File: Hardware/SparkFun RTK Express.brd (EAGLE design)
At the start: 68.2 x 110.1 mm, 168 parts, among them J13 Internal, J17 Qwiic Right Angle, J19 MICRO-SD-PUSH-PUSH-EXT-PIN, J3 USB Female Type C Connector, J4 External, J5 USB Female Type C Connector, Q1 SIL2308-TP, Q2 MBT3904DW1T1, U1 74HC4052D, U10 MCP73833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

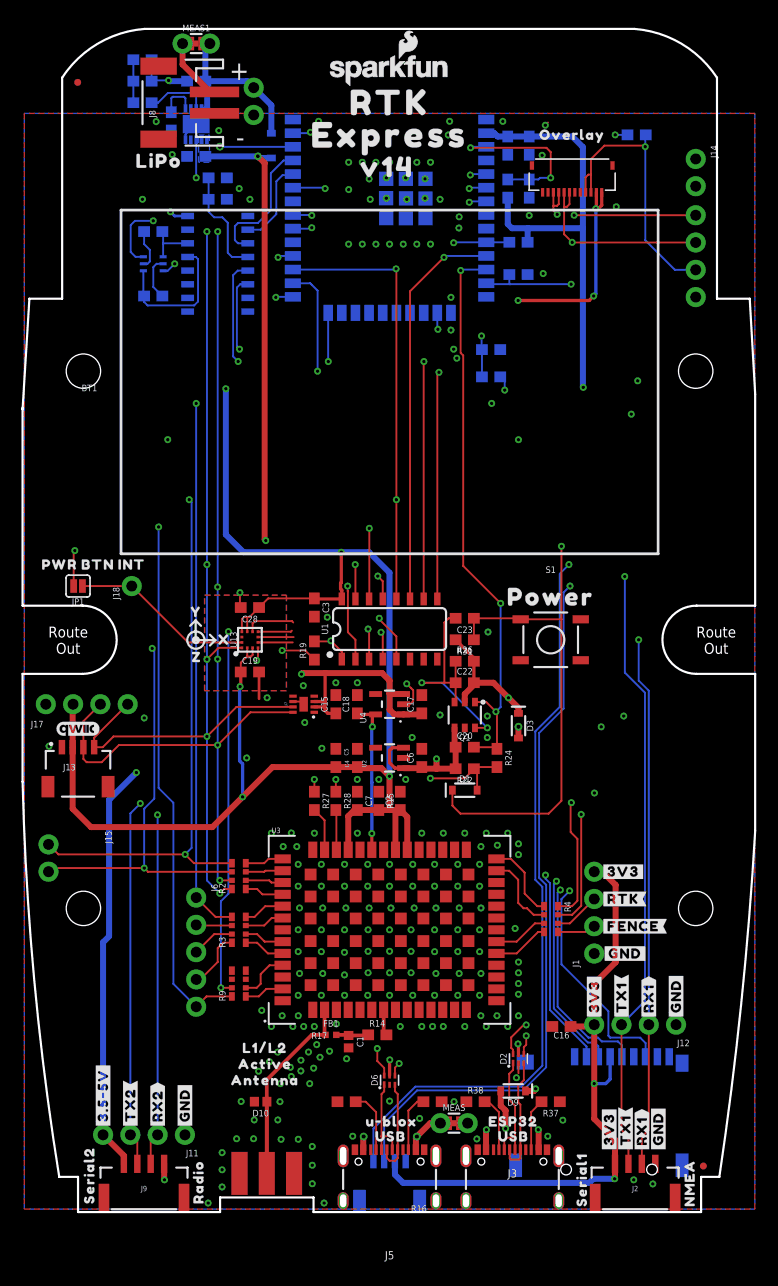
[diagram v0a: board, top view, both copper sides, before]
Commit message: LIF overlay connector, accel plane removal, full ESP32 FP.
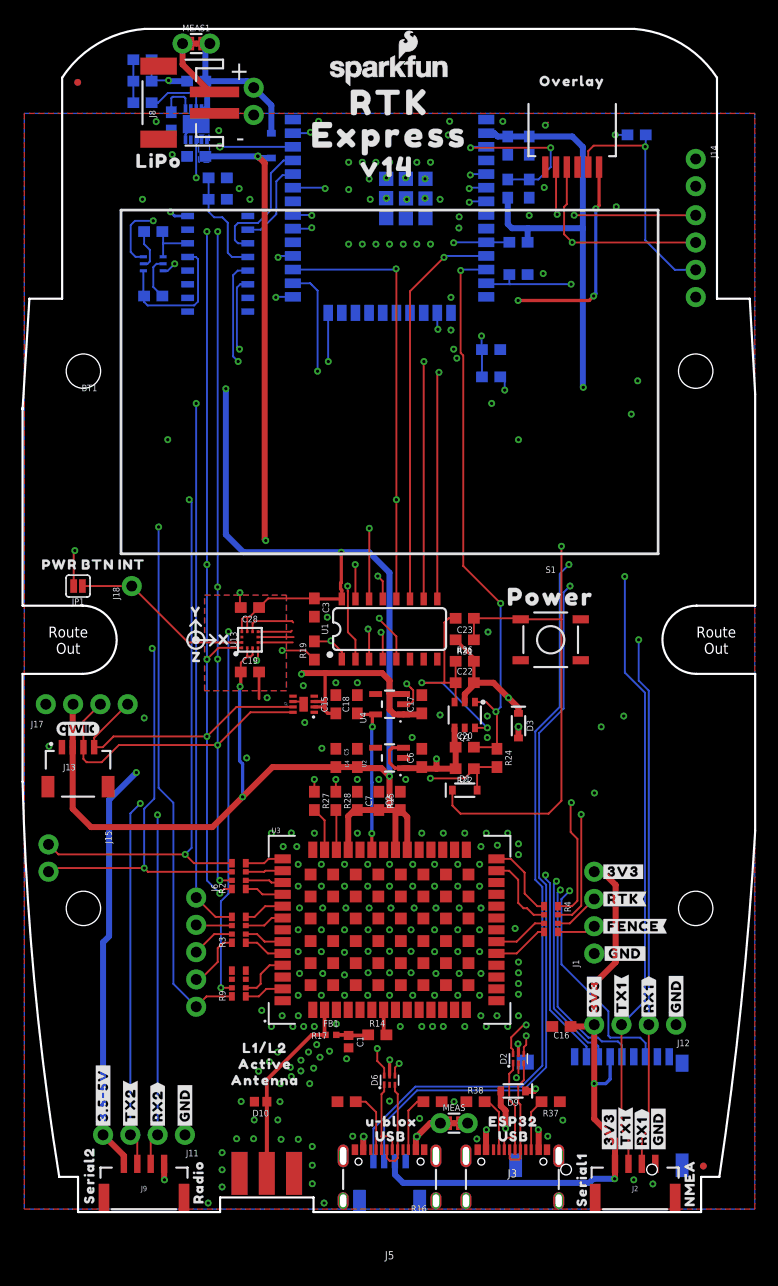
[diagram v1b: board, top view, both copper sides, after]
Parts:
- removed J20: (no value), SparkFun-Connectors:FPC_12_0.5MM
- removed R18: 10k, SparkFun-Resistors:0603@1
- added JP2: CONN_06, 1mm Pitch Connector:FPC_6_1MM-LIF
- added R6: 10k, SparkFun-Resistors:0603
- moved U$8 5.00 mm to (52.0, 105.0)
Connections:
- net CHG_LED_RES: now also JP2.2; no longer J20.3, J20.4
- net CHG_THERM1: now also R6.2; no longer R18.2
- net ESP_14/SETUP_BUTTON: now also JP2.4; no longer J20.7, J20.8
- net GND: now also JP2.6, R6.1; no longer J20.11, J20.12, R18.1
- net POWER_BTN: now also JP2.5; no longer J20.10, J20.9
- net V_USB: now also JP2.1; no longer J20.1, J20.2
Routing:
- net CHG_LED_RES: track 26.4 -> 22.7 mm
- net ESP32_EN: track 76.0 -> 78.2 mm
- net ESP_14/SETUP_BUTTON: track 31.0 -> 31.7 mm
- net POWER_BTN: track 143.0 -> 143.6 mm
- net V_USB: track 189.7 -> 190.2 mm
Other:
- board text added: "ENIG Finish"
- board text removed: "11.9+2.75=14.65mm"
- board text removed: "11.9-3.4=8.5mm actuator length on square button"
- board text removed: "11.9-8=3.9"
- board text removed: "18.5-5-1.6=11.9mm"
- board text removed: "Distance from PCB surface to outer surface of lid:"
- board text removed: "Distance from inner lid to PCB surface:"

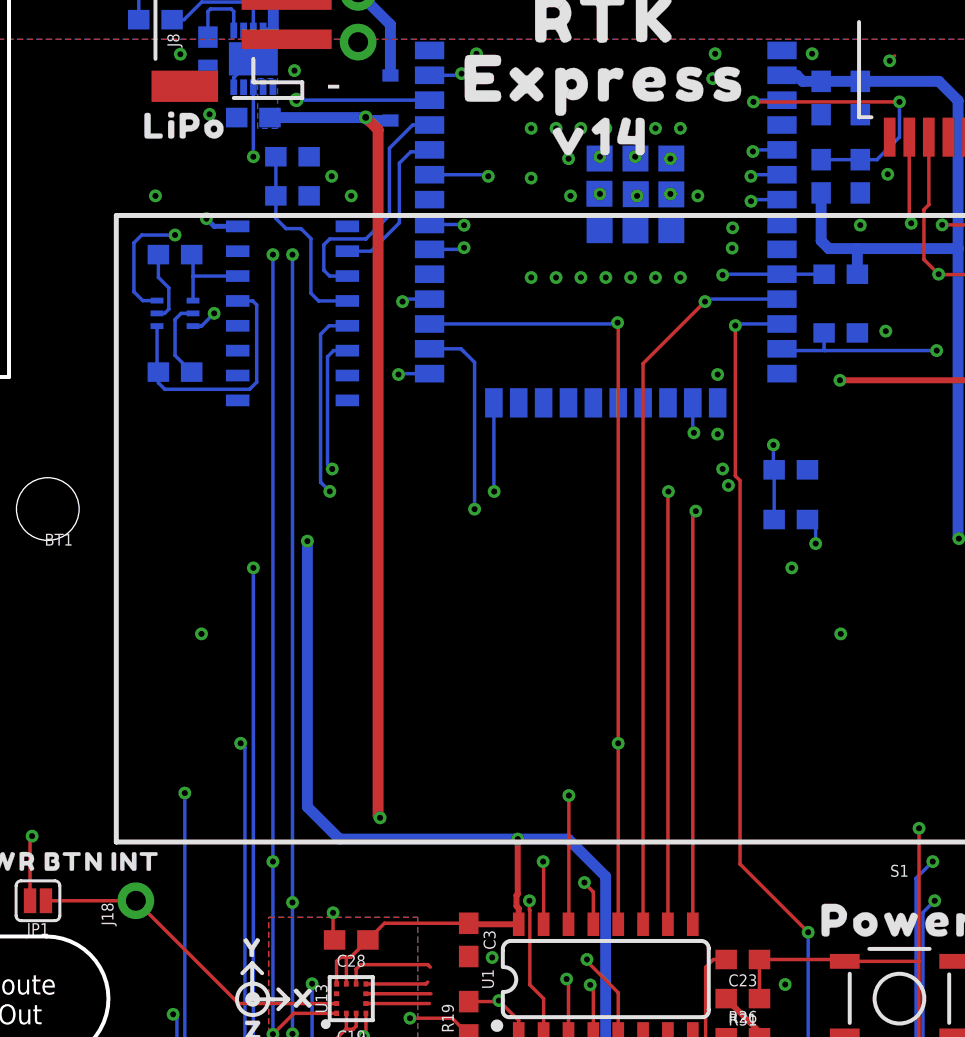
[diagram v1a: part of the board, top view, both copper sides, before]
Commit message: v15. Fix tCream on LIF connector. Correct CH340 3.3V.
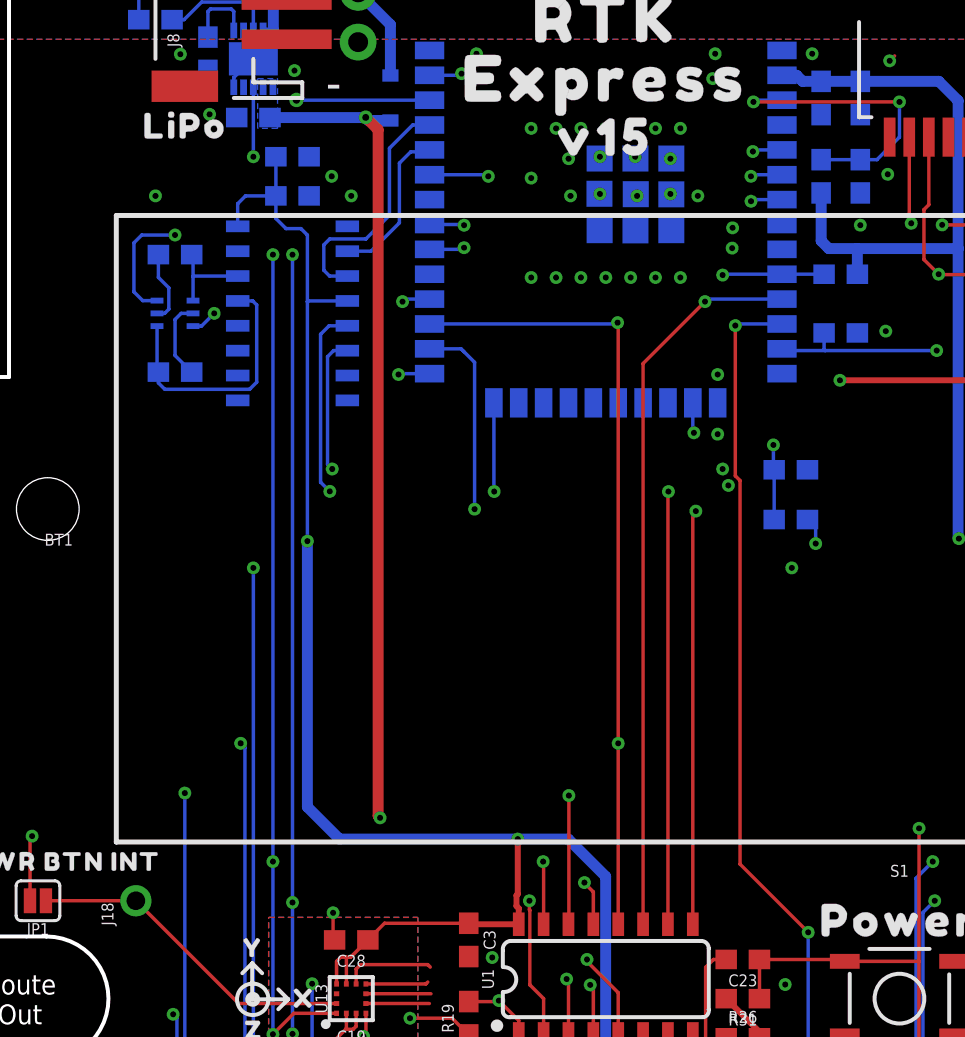
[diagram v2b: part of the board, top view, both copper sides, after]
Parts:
- removed U$12: (no value), output:V140
- added U$18: (no value), output:V150
- J19: value MICRO-SD-PUSH-PUSH-EXT-PIN -> MICROSD
- JP2: value CONN_06 -> (none); device 1mm Pitch Connector:FPC_6_1MM-LIF -> SparkFun-Connectors:FPC_6_1MM-LIF
- MEAS, MEAS1: value JUMPER-COMBO_2_NC_TRACE -> (none)
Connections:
- removed net N$1: C13.1, C14.1, U6.4
- net 3.3V: now also C13.1, C14.1, U6.16, U6.4
- net V_USB: no longer U6.16
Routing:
- net V_USB: track 190.2 -> 134.5 mm, vias 12 -> 9
- net 3.3V: track 308.1 -> 334.2 mm
- net N$1: track 10.2 -> 0.00 mm
- net ESP_I39/ADC39: track 60.8 -> 58.6 mm
- net ESP_I34/ZED_TX_READY: track 103.0 -> 100.7 mm
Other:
- board text added: "N. Seidle"
- board text added: "Red Soldermask"

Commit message: Production files for v15
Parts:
- moved JP2 2.00 mm to (52.0, 98.0)
- moved U$8 2.00 mm to (52.0, 103.0)
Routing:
- net V_USB: track 134.5 -> 132.5 mm
- net POWER_BTN: track 143.6 -> 141.6 mm
- net ESP_14/SETUP_BUTTON: track 31.7 -> 29.7 mm
- net CHG_LED_RES: track 22.7 -> 24.7 mm
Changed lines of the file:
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@@
 <setting verticaltext="up"/>
 </settings>
-<grid distance="0.05" unitdist="inch" unit="inch" style="lines" multiple="1" display="yes" altdistance="0.005" altunitdist="inch" altunit="inch"/>
+<grid distance="1" unitdist="mm" unit="mm" style="lines" multiple="1" display="yes" altdistance="0.1" altunitdist="mm" altunit="mm"/>
 <layers>
 <layer number="1" name="Top/Horz" color="4" fill="1" visible="yes" active="yes"/>
@@
 <layer number="23" name="tOrigins" color="15" fill="1" visible="yes" active="yes"/>
 <layer number="24" name="bOrigins" color="15" fill="1" visible="yes" active="yes"/>
-<layer number="25" name="tNames" color="7" fill="1" visible="yes" active="yes"/>
-<layer number="26" name="bNames" color="7" fill="1" visible="yes" active="yes"/>
-<layer number="27" name="tValues" color="7" fill="1" visible="yes" active="yes"/>
-<layer number="28" name="bValues" color="7" fill="1" visible="yes" active="yes"/>
-<layer number="29" name="tStop" color="7" fill="3" visible="yes" active="yes"/>
-<layer number="30" name="bStop" color="7" fill="6" visible="yes" active="yes"/>
-<layer number="31" name="tCream" color="7" fill="4" visible="yes" active="yes"/>
-<layer number="32" name="bCream" color="7" fill="5" visible="yes" active="yes"/>
-<layer number="33" name="tFinish" color="6" fill="3" visible="yes" active="yes"/>
-<layer number="34" name="bFinish" color="6" fill="6" visible="yes" active="yes"/>
-<layer number="35" name="tGlue" color="7" fill="4" visible="yes" active="yes"/>
-<layer number="36" name="bGlue" color="7" fill="5" visible="yes" active="yes"/>
-<layer number="37" name="tTest" color="7" fill="1" visible="yes" active="yes"/>
-<layer number="38" name="bTest" color="7" fill="1" visible="yes" active="yes"/>
-<layer number="39" name="tKeepout" color="4" fill="11" visible="yes" active="yes"/>
-<layer number="40" name="bKeepout" color="1" fill="11" visible="yes" active="yes"/>
-<layer number="41" name="tRestrict" color="4" fill="10" visible="yes" active="yes"/>
-<layer number="42" name="bRestrict" color="1" fill="10" visible="yes" active="yes"/>
-<layer number="43" name="vRestrict" color="2" fill="10" visible="yes" active="yes"/>
-<layer number="44" name="Drills" color="7" fill="1" visible="yes" active="yes"/>
+<layer number="25" name="tNames" color="7" fill="1" visible="no" active="yes"/>
+<layer number="26" name="bNames" color="7" fill="1" visible="no" active="yes"/>
+<layer number="27" name="tValues" color="7" fill="1" visible="no" active="yes"/>
+<layer number="28" name="bValues" color="7" fill="1" visible="no" active="yes"/>
+<layer number="29" name="tStop" color="7" fill="3" visible="no" active="yes"/>
+<layer number="30" name="bStop" color="7" fill="6" visible="no" active="yes"/>
+<layer number="31" name="tCream" color="7" fill="4" visible="no" active="yes"/>
+<layer number="32" name="bCream" color="7" fill="5" visible="no" active="yes"/>
+<layer number="33" name="tFinish" color="6" fill="3" visible="no" active="yes"/>
+<layer number="34" name="bFinish" color="6" fill="6" visible="no" active="yes"/>
+<layer number="35" name="tGlue" color="7" fill="4" visible="no" active="yes"/>
+<layer number="36" name="bGlue" color="7" fill="5" visible="no" active="yes"/>
+<layer number="37" name="tTest" color="7" fill="1" visible="no" active="yes"/>
+<layer number="38" name="bTest" color="7" fill="1" visible="no" active="yes"/>
+<layer number="39" name="tKeepout" color="4" fill="11" visible="no" active="yes"/>
+<layer number="40" name="bKeepout" color="1" fill="11" visible="no" active="yes"/>
+<layer number="41" name="tRestrict" color="4" fill="10" visible="no" active="yes"/>
+<layer number="42" name="bRestrict" color="1" fill="10" visible="no" active="yes"/>
+<layer number="43" name="vRestrict" color="2" fill="10" visible="no" active="yes"/>
+<layer number="44" name="Drills" color="7" fill="1" visible="no" active="yes"/>
 <layer number="45" name="Holes" color="7" fill="1" visible="yes" active="yes"/>
-<layer number="46" name="Milling" color="3" fill="1" visible="yes" active="yes"/>
-<layer number="47" name="Measures" color="7" fill="1" visible="yes" active="yes"/>
-<layer number="48" name="Document" color="7" fill="1" visible="yes" active="yes"/>
-<layer number="49" name="Reference" color="7" fill="1" visible="yes" active="yes"/>
-<layer number="50" name="dxf" color="7" fill="1" visible="yes" active="yes"/>
+<layer number="46" name="Milling" color="3" fill="1" visible="no" active="yes"/>
+<layer number="47" name="Measures" color="7" fill="1" visible="no" active="yes"/>
+<layer number="48" name="Document" color="7" fill="1" visible="no" active="yes"/>
+<layer number="49" name="Reference" color="7" fill="1" visible="no" active="yes"/>
+<layer number="50" name="dxf" color="7" fill="1" visible="no" active="yes"/>
 <layer number="51" name="tDocu" color="6" fill="1" visible="yes" active="yes"/>
-<layer number="52" name="bDocu" color="7" fill="1" visible="yes" active="yes"/>
+<layer number="52" name="bDocu" color="7" fill="1" visible="no" active="yes"/>
 <layer number="91" name="Nets" color="2" fill="1" visible="no" active="no"/>
 <layer number="92" name="Busses" color="1" fill="1" visible="no" active="no"/>
@@
 <element name="U$4" library="output" package="INT0" value="" x="11" y="60" smashed="yes"/>
 <element name="U$9" library="output" package="PWR_BTN1" value="" x="6" y="60" smashed="yes"/>
-<element name="U$8" library="output" package="OVERLAY0" value="" x="52" y="105" smashed="yes"/>
+<element name="U$8" library="output" package="OVERLAY0" value="" x="52" y="103" smashed="yes"/>
 <element name="D10" library="SparkFun-DiscreteSemi" package="0402" value="PESD0402-0402" x="23" y="10" smashed="yes" rot="R180">
 <attribute name="DIGIKEY_PART" value="PESD0402-140CT-ND" x="23" y="10" size="1.778" layer="27" font="vector" ratio="15" rot="R180" display="off"/>
@@
 <attribute name="VALUE" value="10k" x="44.45" y="78.232" size="0.6096" layer="28" font="vector" ratio="20" rot="MR180" align="top-center"/>
 </element>
-<element name="JP2" library="SparkFun-Connectors" package="FPC_6_1MM-LIF" value="" x="52" y="100" smashed="yes" rot="R180">
-<attribute name="PROD_ID" value="CONN-16692" x="52" y="100" size="1.778" layer="27" rot="R180" display="off"/>
+<element name="JP2" library="SparkFun-Connectors" package="FPC_6_1MM-LIF" value="" x="52" y="98" smashed="yes" rot="R180">
+<attribute name="PROD_ID" value="CONN-16692" x="52" y="98" size="1.778" layer="27" rot="R180" display="off"/>
 </element>
 <element name="R6" library="SparkFun-Resistors" package="0603" value="10k" x="12" y="107" smashed="yes" rot="MR0">
@@
 <contactref element="S1" pad="3"/>
 <via x="57.5" y="74.0031" extent="1-16" drill="0.3048"/>
-<via x="49.4" y="95.1031" extent="1-16" drill="0.3048"/>
+<via x="49.5" y="92.3031" extent="1-16" drill="0.3048"/>
 <via x="32" y="49" extent="1-16" drill="0.3048"/>
 <via x="36.6" y="48.9" extent="1-16" drill="0.3048"/>
@@
 <wire x1="44.09" y1="86.1" x2="44.323" y2="86.1" width="0.3048" layer="16"/>
 <contactref element="JP2" pad="4"/>
-<wire x1="51.5" y1="97" x2="51.5" y2="93.55" width="0.1778" layer="1"/>
+<wire x1="51.5" y1="95" x2="51.5" y2="93.55" width="0.1778" layer="1"/>
 <wire x1="51.5" y1="93.55" x2="51.25" y2="93.3" width="0.1778" layer="1"/>
 </signal>
@@
 <contactref element="JP2" pad="2"/>
 <contactref element="R1" pad="1"/>
-<wire x1="53.5" y1="97" x2="53.5" y2="98.5" width="0.1778" layer="1"/>
+<wire x1="53.5" y1="95" x2="53.5" y2="98.5" width="0.1778" layer="1"/>
 <wire x1="53.5" y1="98.5" x2="54" y2="99" width="0.1778" layer="1"/>
 <wire x1="54" y1="99" x2="58.7" y2="99" width="0.1778" layer="1"/>
@@
 <wire x1="51" y1="61.7" x2="51" y2="92.52" width="0.1778" layer="15"/>
 <contactref element="JP2" pad="5"/>
-<wire x1="50.5" y1="97" x2="50.5" y2="92.7" width="0.1778" layer="1"/>
+<wire x1="50.5" y1="95" x2="50.5" y2="92.7" width="0.1778" layer="1"/>
 <wire x1="50.5" y1="92.7" x2="50.6" y2="92.6" width="0.1778" layer="1"/>
 </signal>
@@
 <wire x1="35" y1="12.43" x2="35" y2="13.874" width="0.3048" layer="1"/>
 <wire x1="35" y1="13.874" x2="35.02" y2="13.894" width="0.3048" layer="1"/>
-<wire x1="47" y1="44.9" x2="47" y2="71.628" width="0.3048" layer="15"/>
-<wire x1="47" y1="71.628" x2="47" y2="84.5424" width="0.3048" layer="15"/>
+<wire x1="47" y1="44.9" x2="47" y2="84.5424" width="0.3048" layer="15"/>
 <wire x1="47" y1="84.5424" x2="46.9604" y2="84.582" width="0.3048" layer="15"/>
 <via x="46.9604" y="84.582" extent="1-16" drill="0.3048"/>
@@
 <wire x1="54.2" y1="85.2" x2="54" y2="85" width="0.3048" layer="16"/>
 <contactref element="JP2" pad="1"/>
-<wire x1="54.5" y1="97" x2="54.5" y2="93.4169" width="0.3048" layer="1"/>
+<wire x1="54.5" y1="95" x2="54.5" y2="93.4169" width="0.3048" layer="1"/>
 <wire x1="54.5" y1="93.4169" x2="54.2" y2="93.1169" width="0.3048" layer="1"/>
 </signal>
